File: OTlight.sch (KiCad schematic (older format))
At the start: 61 parts, among them P1 CONN_01X01, Q1 TEMT6000, Q2 Q_NMOS_GSD, T1 TRANSFO, U1 LM3478, U10 IN-14, U11 IN-14, U12 MAX6931, U13 IN-14, U2 NodeMCU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

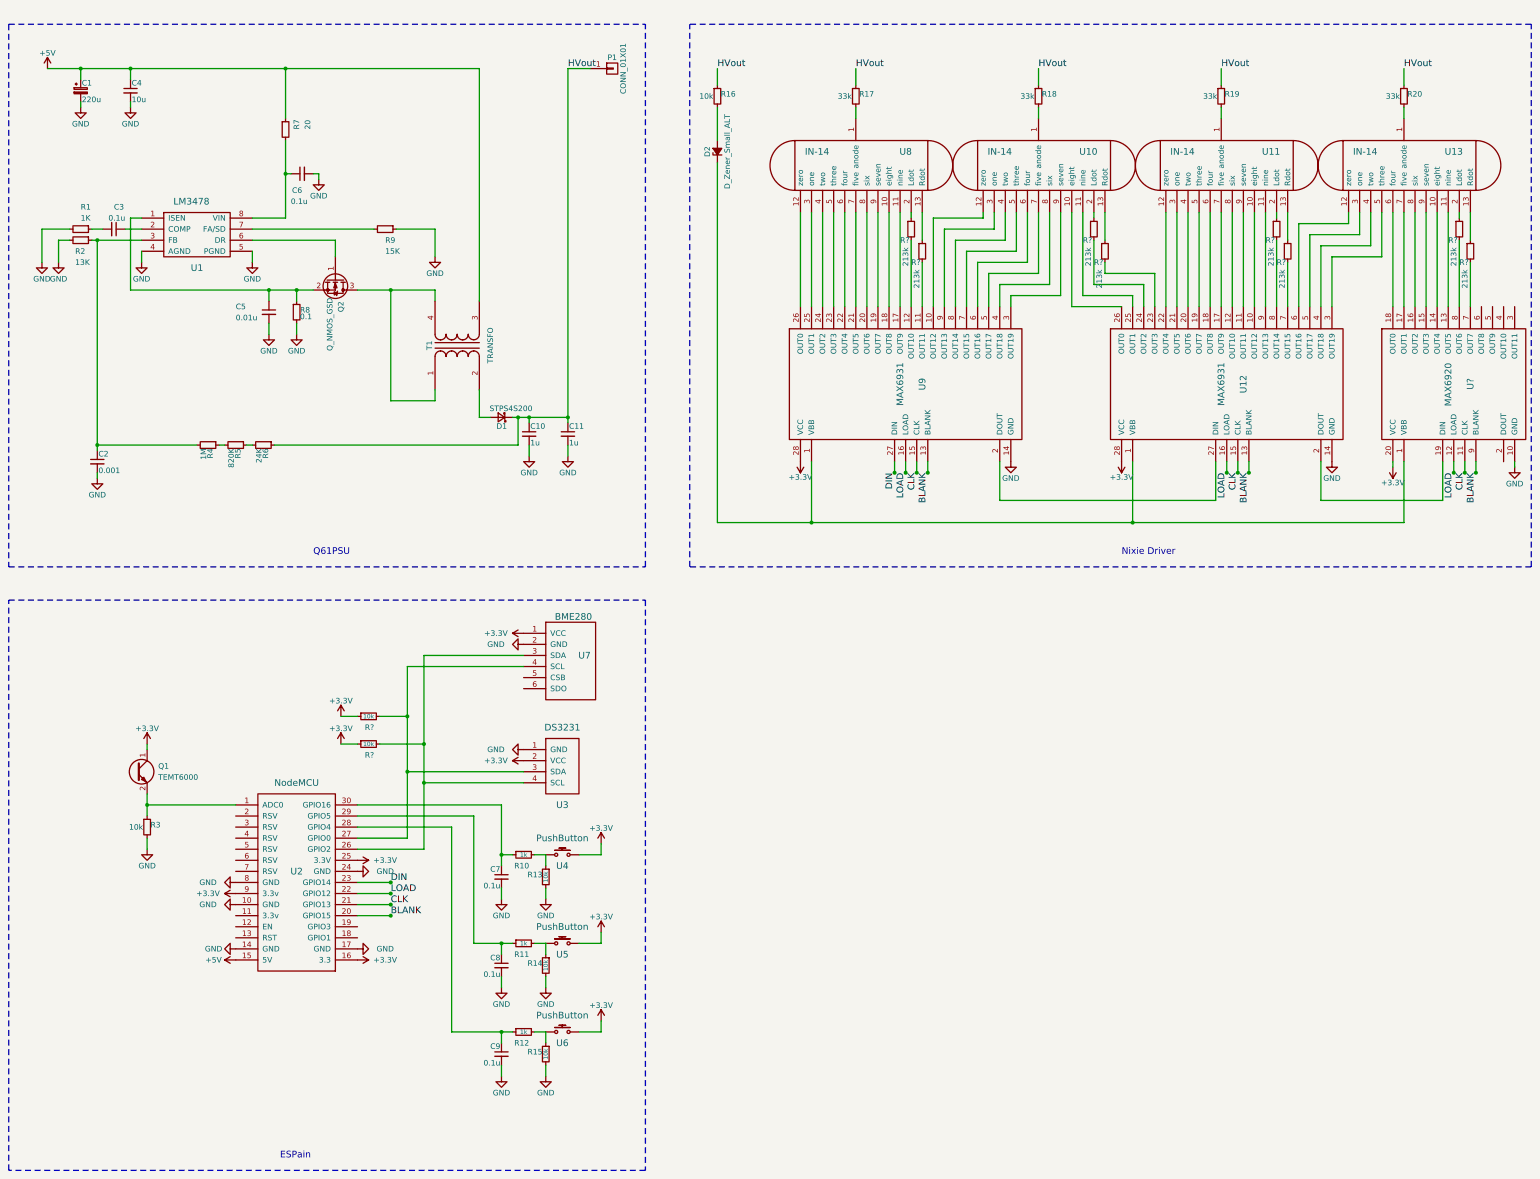
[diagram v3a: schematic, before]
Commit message: Fixes + PCB created
Fixed buttons generated PCB+ started rough laying
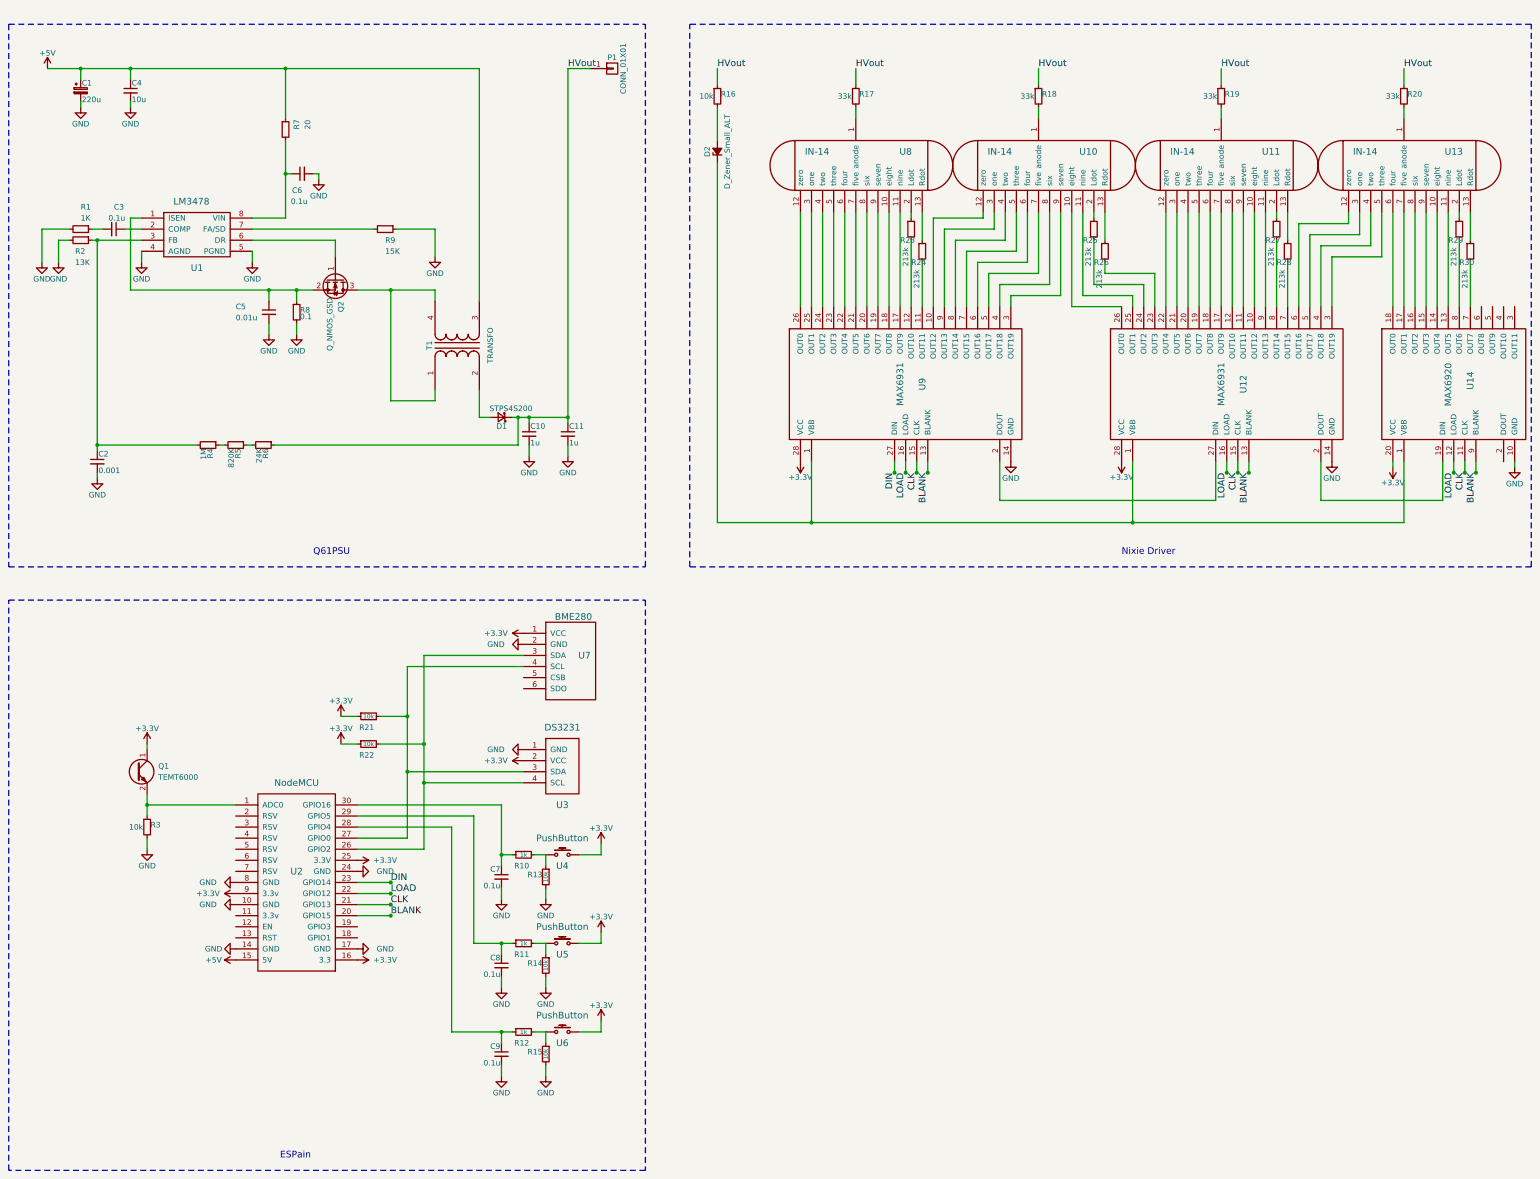
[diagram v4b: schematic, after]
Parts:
- D2: footprint (none) -> Diodes_SMD:D_SOD-123
- P1: footprint (none) -> Connect:1pin
- Q1: footprint (none) -> BamboulabFootprints:TEMT6000
- R10, R11, R12, R13, R14, R15, R16, R17, R18, R19, R20: footprint (none) -> Resistors_SMD:R_0805_HandSoldering
- R21, R22, R23, R24, R25, R26, R27, R28, R29, R30: renamed from R?; footprint (none) -> Resistors_SMD:R_0805_HandSoldering
- R3: footprint (none) -> Capacitors_SMD:C_0805_HandSoldering
- U10, U11, U13, U8: footprint (none) -> BamboulabFootprints:IN-14
- U12, U9: footprint (none) -> BamboulabFootprints:SW-28
- U14: renamed from U?; footprint (none) -> BamboulabFootprints:SW-20
- U2: footprint (none) -> BamboulabFootprints:NodeMCU-V2
- U4, U5, U6: footprint (none) -> BamboulabFootprints:SPEH120100
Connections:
- net +3V3: now also U4.2, U5.2, U6.2; no longer U4.1, U5.1, U6.1
- net at R10.2, R13.1: now also U4.1; no longer U4.2
- net at R11.2, R14.1: now also U5.1; no longer U5.2
- net at R12.2, R15.1: now also U6.1; no longer U6.2

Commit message: Components fitted
Everything fits!
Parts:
- C1: footprint Capacitors_SMD:c_elec_6.3x7.7 -> Capacitors_SMD:CP_Elec_6.3x7.7
- D1: footprint Diodes_SMD:SMB_Handsoldering -> Diodes_SMD:D_SMB_Handsoldering
- P1: footprint Connect:1pin -> Connect:PINTST
- U3: footprint (none) -> BamboulabFootprints:DS3231
- U7: footprint (none) -> BamboulabFootprints:BME280
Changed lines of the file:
@@
 F 0 "C1" H 1360 1320 50  0000 L CNN
 F 1 "220u" H 1360 1170 50  0000 L CNN
-F 2 "Capacitors_SMD:c_elec_6.3x7.7" H 1350 1250 50  0001 C CNN
+F 2 "Capacitors_SMD:CP_Elec_6.3x7.7" H 1350 1250 50  0001 C CNN
 F 3 "" H 1350 1250 50  0000 C CNN
 	1    1350 1250
@@
 F 0 "D1" H 5100 4280 50  0000 L CNN
 F 1 "STPS4S200" H 4870 4120 50  0000 L CNN
-F 2 "Diodes_SMD:SMB_Handsoldering" V 5150 4200 50  0001 C CNN
+F 2 "Diodes_SMD:D_SMB_Handsoldering" V 5150 4200 50  0001 C CNN
 F 3 "" V 5150 4200 50  0000 C CNN
 	1    5150 4200
@@
 F 0 "U7" H 5900 6650 60  0000 C CNN
 F 1 "BME280" H 5800 7000 60  0000 C CNN
-F 2 "" H 5800 6500 60  0001 C CNN
+F 2 "BamboulabFootprints:BME280" H 5800 6500 60  0001 C CNN
 F 3 "" H 5800 6500 60  0001 C CNN
 	1    5800 6500
@@
 F 0 "U3" H 5700 7000 60  0000 C CNN
 F 1 "DS3231" H 5700 7700 60  0000 C CNN
-F 2 "" H 5550 7300 60  0001 C CNN
+F 2 "BamboulabFootprints:DS3231" H 5550 7300 60  0001 C CNN
 F 3 "" H 5550 7300 60  0001 C CNN
 	1    5700 7350
@@
 F 0 "P1" H 6150 1150 50  0000 C CNN
 F 1 "CONN_01X01" V 6250 1050 50  0000 C CNN
-F 2 "Connect:1pin" H 6150 1050 50  0001 C CNN
+F 2 "Connect:PINTST" H 6150 1050 50  0001 C CNN
 F 3 "" H 6150 1050 50  0000 C CNN
 	1    6150 1050

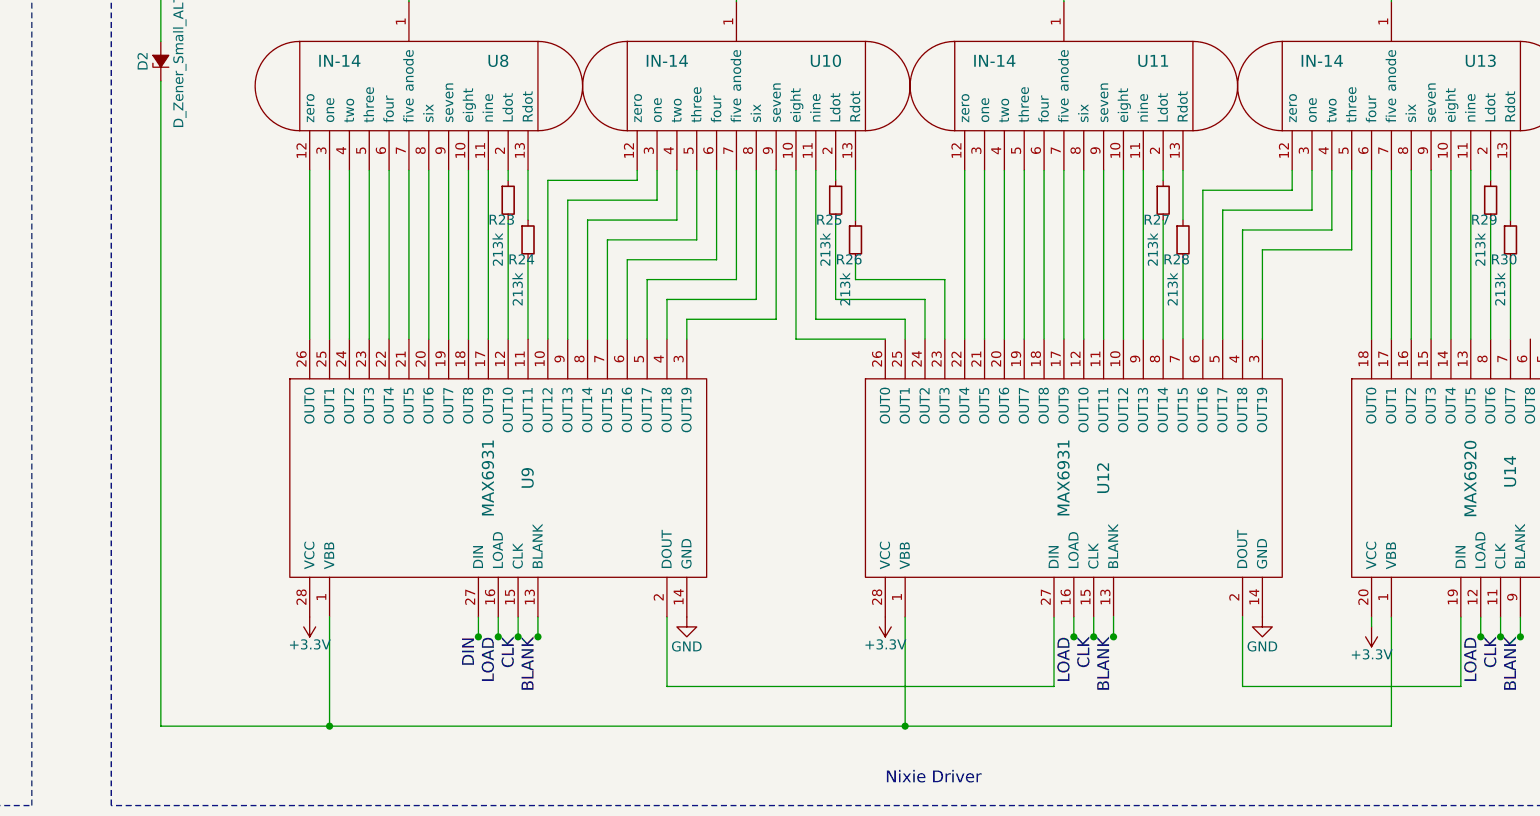
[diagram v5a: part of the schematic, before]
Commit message: Board size to fit Altoids+ decoupling caps
NOTHING IS WHERE IT SHOULD BE
EVERYTHING IS WRONG
I AM GOING TO BED!
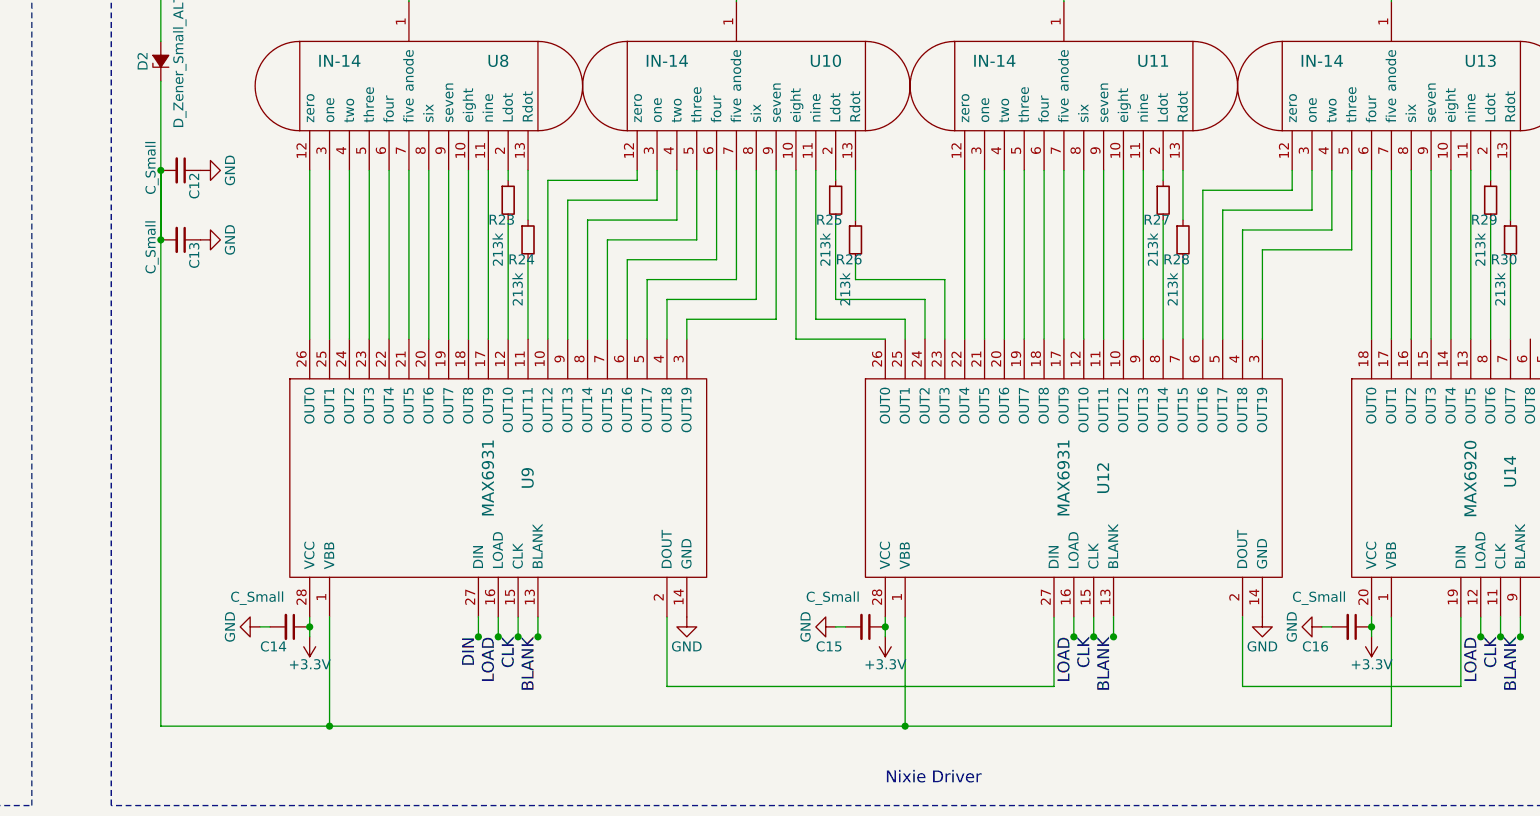
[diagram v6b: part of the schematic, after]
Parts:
- added C12, C13, C14, C15, C16: C_Small, Capacitors_SMD:C_0805_HandSoldering, symbol C_Small
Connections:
- net +3V3: now also C14.1, C15.1, C16.1
- net GND: now also C12.1, C13.1, C14.2, C15.2, C16.2
- net at D2.1 (K), U12.1 (VBB), U14.1 (VBB)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: now also C12.2, C13.2
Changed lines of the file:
@@
 L +3.3V #PWR024
 U 1 1 5872E748
-P 7850 4600
-F 0 "#PWR024" H 7850 4450 50  0001 C CNN
-F 1 "+3.3V" H 7850 4740 50  0000 C CNN
-F 2 "" H 7850 4600 50  0000 C CNN
-F 3 "" H 7850 4600 50  0000 C CNN
-	1    7850 4600
+P 7850 4700
+F 0 "#PWR024" H 7850 4550 50  0001 C CNN
+F 1 "+3.3V" H 7850 4840 50  0000 C CNN
+F 2 "" H 7850 4700 50  0000 C CNN
+F 3 "" H 7850 4700 50  0000 C CNN
+	1    7850 4700
 	-1   0    0    1
 $EndComp
@@
 L +3.3V #PWR043
 U 1 1 5872F33F
-P 10750 4600
-F 0 "#PWR043" H 10750 4450 50  0001 C CNN
-F 1 "+3.3V" H 10750 4740 50  0000 C CNN
-F 2 "" H 10750 4600 50  0000 C CNN
-F 3 "" H 10750 4600 50  0000 C CNN
-	1    10750 4600
+P 10750 4700
+F 0 "#PWR043" H 10750 4550 50  0001 C CNN
+F 1 "+3.3V" H 10750 4840 50  0000 C CNN
+F 2 "" H 10750 4700 50  0000 C CNN
+F 3 "" H 10750 4700 50  0000 C CNN
+	1    10750 4700
 	-1   0    0    1
 $EndComp
@@
 L +3.3V #PWR046
 U 1 1 5884849A
-P 13200 4650
-F 0 "#PWR046" H 13200 4500 50  0001 C CNN
-F 1 "+3.3V" H 13200 4790 50  0000 C CNN
-F 2 "" H 13200 4650 50  0000 C CNN
-F 3 "" H 13200 4650 50  0000 C CNN
-	1    13200 4650
+P 13200 4700
+F 0 "#PWR046" H 13200 4550 50  0001 C CNN
+F 1 "+3.3V" H 13200 4840 50  0000 C CNN
+F 2 "" H 13200 4700 50  0000 C CNN
+F 3 "" H 13200 4700 50  0000 C CNN
+	1    13200 4700
 	-1   0    0    1
 $EndComp
 Wire Wire Line
-	13200 4650 13200 4600
+	13200 4600 13200 4700
 Wire Wire Line
 	14300 4650 14300 4600
@@
 	1    0    0    -1
 $EndComp
+$Comp
+L C_Small C12
+U 1 1 58D75024
+P 7200 2350
+F 0 "C12" H 7210 2420 50  0000 L CNN
+F 1 "C_Small" H 7050 2200 50  0000 L CNN
+F 2 "Capacitors_SMD:C_0805_HandSoldering" H 7200 2350 50  0001 C CNN
+F 3 "" H 7200 2350 50  0000 C CNN
+	1    7200 2350
+	0    1    1    0
+$EndComp
+$Comp
+L C_Small C13
+U 1 1 58D75379
+P 7200 2700
+F 0 "C13" H 7210 2770 50  0000 L CNN
+F 1 "C_Small" H 7100 2550 50  0000 L CNN
+F 2 "Capacitors_SMD:C_0805_HandSoldering" H 7200 2700 50  0001 C CNN
+F 3 "" H 7200 2700 50  0000 C CNN
+	1    7200 2700
+	0    1    1    0
+$EndComp
+$Comp
+L GND #PWR047
+U 1 1 58D767C7
+P 7300 2350
+F 0 "#PWR047" H 7300 2100 50  0001 C CNN
+F 1 "GND" H 7300 2200 50  0000 C CNN
+F 2 "" H 7300 2350 50  0000 C CNN
+F 3 "" H 7300 2350 50  0000 C CNN
+	1    7300 2350
+	0    -1   -1   0
+$EndComp
+$Comp
+L GND #PWR048
+U 1 1 58D76C7F
+P 7300 2700
+F 0 "#PWR048" H 7300 2450 50  0001 C CNN
+F 1 "GND" H 7300 2550 50  0000 C CNN
+F 2 "" H 7300 2700 50  0000 C CNN
+F 3 "" H 7300 2700 50  0000 C CNN
+	1    7300 2700
+	0    -1   -1   0
+$EndComp
+Wire Wire Line
+	7850 4600 7850 4700
+Wire Wire Line
+	10750 4600 10750 4700
+$Comp
+L C_Small C14
+U 1 1 58D7E4CA
+P 7750 4650
+F 0 "C14" V 7850 4500 50  0000 L CNN
+F 1 "C_Small" V 7600 4350 50  0000 L CNN
+F 2 "Capacitors_SMD:C_0805_HandSoldering" H 7750 4650 50  0001 C CNN
+F 3 "" H 7750 4650 50  0000 C CNN
+	1    7750 4650
+	0    1    1    0
+$EndComp
+$Comp
+L C_Small C15
+U 1 1 58D7E5D4
+P 10650 4650
+F 0 "C15" V 10750 4400 50  0000 L CNN
+F 1 "C_Small" V 10500 4350 50  0000 L CNN
+F 2 "Capacitors_SMD:C_0805_HandSoldering" H 10650 4650 50  0001 C CNN
+F 3 "" H 10650 4650 50  0000 C CNN
+	1    10650 4650
+	0    1    1    0
+$EndComp
+$Comp
+L C_Small C16
+U 1 1 58D7EB6B
+P 13100 4650
+F 0 "C16" V 13200 4400 50  0000 L CNN
+F 1 "C_Small" V 12950 4350 50  0000 L CNN
+F 2 "Capacitors_SMD:C_0805_HandSoldering" H 13100 4650 50  0001 C CNN
+F 3 "" H 13100 4650 50  0000 C CNN
+	1    13100 4650
+	0    1    1    0
+$EndComp
+$Comp
+L GND #PWR049
+U 1 1 58D7F219
+P 7600 4650
+F 0 "#PWR049" H 7600 4400 50  0001 C CNN
+F 1 "GND" H 7600 4500 50  0000 C CNN
+F 2 "" H 7600 4650 50  0000 C CNN
+F 3 "" H 7600 4650 50  0000 C CNN
+	1    7600 4650
+	0    1    1    0
+$EndComp
+Wire Wire Line
+	7600 4650 7650 4650
+$Comp
+L GND #PWR050
+U 1 1 58D8108A
+P 10500 4650
+F 0 "#PWR050" H 10500 4400 50  0001 C CNN
+F 1 "GND" H 10500 4500 50  0000 C CNN
+F 2 "" H 10500 4650 50  0000 C CNN
+F 3 "" H 10500 4650 50  0000 C CNN
+	1    10500 4650
+	0    1    1    0
+$EndComp
+Wire Wire Line
+	10500 4650 10550 4650
+$Comp
+L GND #PWR051
+U 1 1 58D87A8C
+P 12950 4650
+F 0 "#PWR051" H 12950 4400 50  0001 C CNN
+F 1 "GND" H 12950 4500 50  0000 C CNN
+F 2 "" H 12950 4650 50  0000 C CNN
+F 3 "" H 12950 4650 50  0000 C CNN
+	1    12950 4650
+	0    1    1    0
+$EndComp
+Wire Wire Line
+	12950 4650 13000 4650
+Connection ~ 7850 4650
+Connection ~ 10750 4650
+Connection ~ 13200 4650
+Wire Wire Line
+	7100 2700 7100 2350
+Connection ~ 7100 2350
+Connection ~ 7100 2700
 $EndSCHEMATC

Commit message: Updated PCB and footprints - Changed footprints for angled pins SMD package - Repositioned holes - Locked Altoids shaped outline, holes, tubes and modules - Changed R3 for resistor package (was 0805 but as capacitor)
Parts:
- R3: footprint Capacitors_SMD:C_0805_HandSoldering -> Resistors_SMD:R_0805_HandSoldering
- U2: footprint BamboulabFootprints:NodeMCU-V2 -> BamboulabFootprints:NodeMCU-V3
- U3: footprint BamboulabFootprints:DS3231 -> BamboulabFootprints:DS3231-Angled
- U7: footprint BamboulabFootprints:BME280 -> BamboulabFootprints:BME280-Angled
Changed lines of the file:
@@
 LIBS:contrib
 LIBS:valves
-LIBS:bambouLab
 LIBS:OTlight-cache
 EELAYER 25 0
@@
 F 0 "U2" H 3300 8400 60  0000 C CNN
 F 1 "NodeMCU" H 3300 9200 60  0000 C CNN
-F 2 "BamboulabFootprints:NodeMCU-V2" H 3400 8600 60  0001 C CNN
+F 2 "BamboulabFootprints:NodeMCU-V3" H 3400 8600 60  0001 C CNN
 F 3 "" H 3400 8600 60  0001 C CNN
 	1    3300 8350
@@
 F 0 "U7" H 5900 6650 60  0000 C CNN
 F 1 "BME280" H 5800 7000 60  0000 C CNN
-F 2 "BamboulabFootprints:BME280" H 5800 6500 60  0001 C CNN
+F 2 "BamboulabFootprints:BME280-Angled" H 5800 6500 60  0001 C CNN
 F 3 "" H 5800 6500 60  0001 C CNN
 	1    5800 6500
@@
 F 0 "U3" H 5700 7000 60  0000 C CNN
 F 1 "DS3231" H 5700 7700 60  0000 C CNN
-F 2 "BamboulabFootprints:DS3231" H 5550 7300 60  0001 C CNN
+F 2 "BamboulabFootprints:DS3231-Angled" H 5550 7300 60  0001 C CNN
 F 3 "" H 5550 7300 60  0001 C CNN
 	1    5700 7350
@@
 F 0 "R3" H 1980 7920 50  0000 L CNN
 F 1 "R_Small" H 1980 7860 50  0001 L CNN
-F 2 "Capacitors_SMD:C_0805_HandSoldering" H 1950 7900 50  0001 C CNN
+F 2 "Resistors_SMD:R_0805_HandSoldering" H 1950 7900 50  0001 C CNN
 F 3 "10k" H 1850 7900 50  0000 C CNN
 	1    1950 7900
